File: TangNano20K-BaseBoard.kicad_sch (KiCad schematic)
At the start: 0 parts

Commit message: Add electronic schematic
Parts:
- added D1, D2, D3, D4: LED, symbol Device:LED
- added J1, J2: Conn_01x20_Socket, symbol Connector:Conn_01x20_Socket
- added J3, J4: Conn_01x06_Socket, symbol Connector:Conn_01x06_Socket
- added Q1, Q2, Q3, Q4: PN2222A, Package_TO_SOT_THT:TO-92_Inline, symbol Transistor_BJT:PN2222A
- added R1, R2, R3, R4, R5, R6, R7, R8: 220R, symbol Device:R
- added R10, R11, R12, R13, R14, R15, R16, R9: 330R, symbol Device:R
- added R19, R20, R21, R22, R23, R24, R25, R26, R27, R28: 10k, symbol Device:R
- added SW1, SW2, SW3, SW4, SW9: SW_SPDT_321, symbol Switch:SW_SPDT_321
- added SW5, SW6, SW7, SW8: SW_Push, symbol Switch:SW_Push
- added U1: CC56-12EWA, Display_7Segment:CA56-12EWA, symbol Display_Character:CC56-12EWA
- added U2: SSD1306, symbol MySymbols:SSD1306
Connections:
- new net: D1.2 (A), R13.2
- new net: R27.1, R28.2, SW9.1 (C), U2.2 (VCC)
- new net: Q2.2 (B), R10.1
- new net: Q1.2 (B), R9.1
- new net: Q4.2 (B), R12.1
- new net: D4.2 (A), R16.2
- new net: Q3.2 (B), R11.1
- new net: D2.2 (A), R14.2
- new net: D3.2 (A), R15.2
- new net +3V3: J1.19 (Pin_19), J2.16 (Pin_16), J3.5 (Pin_5), J4.5 (Pin_5), SW1.2 (B), SW2.2 (B), SW3.2 (B), SW4.2 (B), SW5.1, SW6.1, SW7.1, SW8.1, SW9.2 (B)
- new net +5V: J2.1 (Pin_1)
- new net 15: J1.6 (Pin_6), R13.1
- new net 16: J1.7 (Pin_7), R14.1
- new net 17: J1.15 (Pin_15), R15.1
- new net 18: J1.18 (Pin_18), R16.1
- new net 19: J1.17 (Pin_17), R27.2, U2.3 (SCL)
- new net 20: J1.16 (Pin_16), R28.1, U2.4 (SDA)
- new net 25: J1.10 (Pin_10), R3.1
- new net 26: J1.11 (Pin_11), R4.1
- new net 27: J1.8 (Pin_8), R1.1
- new net 28: J1.9 (Pin_9), R2.1
- new net 29: J1.12 (Pin_12), R5.1
- new net 30: J1.13 (Pin_13), R6.1
- new net 31: J1.14 (Pin_14), R7.1
- new net 41: J2.6 (Pin_6), J3.2 (Pin_2)
- new net 42: J2.5 (Pin_5), R8.1
- new net 48: J2.10 (Pin_10), R12.2
- new net 49: J2.12 (Pin_12), J3.4 (Pin_4)
- new net 51: J2.9 (Pin_9), R11.2
- new net 52: J2.20 (Pin_20), J4.4 (Pin_4)
- new net 53: J2.19 (Pin_19), J4.3 (Pin_3)
- new net 54: J2.8 (Pin_8), R10.2
- new net 55: J2.11 (Pin_11), J3.3 (Pin_3)
- new net 56: J2.7 (Pin_7), R9.2
- new net 71: J2.18 (Pin_18), R19.2, SW1.1 (C)
- new net 72: J2.17 (Pin_17), R20.2, SW2.1 (C)
- new net 73: J1.1 (Pin_1), R21.2, SW3.1 (C)
- new net 74: J1.2 (Pin_2), R22.2, SW4.1 (C)
- new net 75: J1.3 (Pin_3), R23.2, SW5.2
- new net 76: J2.3 (Pin_3), R24.2, SW6.2
- new net 77: J1.5 (Pin_5), R25.2, SW7.2
- new net 79: J2.14 (Pin_14), J4.2 (Pin_2)
- new net 80: J2.4 (Pin_4), J3.1 (Pin_1)
- new net 85: J1.4 (Pin_4), R26.2, SW8.2
- new net 86: J2.13 (Pin_13), J4.1 (Pin_1)
- new net CC1: Q1.3 (C), U1.12 (CC1)
- new net CC2: Q2.3 (C), U1.9 (CC2)
- new net CC3: Q3.3 (C), U1.8 (CC3)
- new net CC4: Q4.3 (C), U1.6 (CC4)
- new net DPX: R8.2, U1.3 (DPX)
- new net GND: D1.1 (K), D2.1 (K), D3.1 (K), D4.1 (K), J1.20 (Pin_20), J2.15 (Pin_15), J2.2 (Pin_2), J3.6 (Pin_6), J4.6 (Pin_6), Q1.1 (E), Q2.1 (E), Q3.1 (E), Q4.1 (E), R19.1, R20.1, R21.1, R22.1, R23.1, R24.1, R25.1, R26.1, U2.1 (GND)
- new net a: R1.2, U1.11 (a)
- new net b: R2.2, U1.7 (b)
- new net c: R3.2, U1.4 (c)
- new net d: R4.2, U1.2 (d)
- new net e: R5.2, U1.1 (e)
- new net f: R6.2, U1.10 (f)
- new net g: R7.2, U1.5 (g)
- no-connect marks 0 -> 5
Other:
- note added: "4-Digit 7-Segment Display"
- note added: "GPIO Expansion Headers"
- note added: "OLED Display (I2C)"
- note added: "Push Buttons"
- note added: "Slide Switches"
- note added: "Tang Nano 20K Connectors"
- note added: "User LEDs"

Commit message: Add footprint for electronic element
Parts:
- J1, J2: footprint (none) -> Connector_PinSocket_2.54mm:PinSocket_1x20_P2.54mm_Vertical
- J3, J4: footprint (none) -> Connector_PinSocket_2.54mm:PinSocket_1x06_P2.54mm_Vertical
- LED_1: renamed from D1; footprint (none) -> LED_SMD:LED_0805_2012Metric_Pad1.15x1.40mm_HandSolder
- LED_2: renamed from D2; footprint (none) -> LED_SMD:LED_0805_2012Metric_Pad1.15x1.40mm_HandSolder
- LED_3: renamed from D3; footprint (none) -> LED_SMD:LED_0805_2012Metric_Pad1.15x1.40mm_HandSolder
- LED_4: renamed from D4; footprint (none) -> LED_SMD:LED_0805_2012Metric_Pad1.15x1.40mm_HandSolder
- Push_Button_1: renamed from SW5; footprint (none) -> Button_Switch_SMD:SW_Push_1TS009xxxx-xxxx-xxxx_6x6x5mm
- Push_Button_2: renamed from SW6; footprint (none) -> Button_Switch_SMD:SW_Push_1TS009xxxx-xxxx-xxxx_6x6x5mm
- Push_Button_3: renamed from SW7; footprint (none) -> Button_Switch_SMD:SW_Push_1TS009xxxx-xxxx-xxxx_6x6x5mm
- Push_Button_4: renamed from SW8; footprint (none) -> Button_Switch_SMD:SW_Push_1TS009xxxx-xxxx-xxxx_6x6x5mm
- Q1, Q2, Q3, Q4: footprint Package_TO_SOT_THT:TO-92_Inline -> Package_TO_SOT_SMD:SOT-23
- R1, R10, R11, R12, R13, R14, R15, R16, R19, R2, R20, R21, R22, R23, R24, R25, R26, R27, R28, R3, R4, R5, R6, R7, R8, R9: footprint (none) -> Resistor_SMD:R_0805_2012Metric_Pad1.20x1.40mm_HandSolder
- Slide_Switch_1: renamed from SW1; footprint (none) -> MyFootPrints:SL19121
- Slide_Switch_2: renamed from SW2; footprint (none) -> MyFootPrints:SL19121
- Slide_Switch_3: renamed from SW3; footprint (none) -> MyFootPrints:SL19121
- Slide_Switch_4: renamed from SW4; footprint (none) -> MyFootPrints:SL19121
- Slide_Switch_OLED1: renamed from SW9; footprint (none) -> MyFootPrints:SL19121
- U2: footprint (none) -> MyFootPrints:128x64OLED

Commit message: Update schematic, add new symbol, footprint and 3d model
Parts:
- removed Push_Button_1, Push_Button_2, Push_Button_3, Push_Button_4: SW_Push, Button_Switch_SMD:SW_Push_1TS009xxxx-xxxx-xxxx_6x6x5mm, symbol Switch:SW_Push
- added S1, S2, S3, S4: 1301.9315, MyFootPrints:13019319, symbol MySymbols:1301.9315
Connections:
- net +3V3: now also S1.1 (NO_1), S2.1 (NO_1), S3.1 (NO_1), S4.1 (NO_1)
- net 75: now also S1.4 (COM_2)
- net 76: now also S2.4 (COM_2)
- net 77: now also S3.4 (COM_2)
- net 85: now also S4.4 (COM_2)
- no-connect marks 5 -> 13
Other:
- moved on the sheet: R23

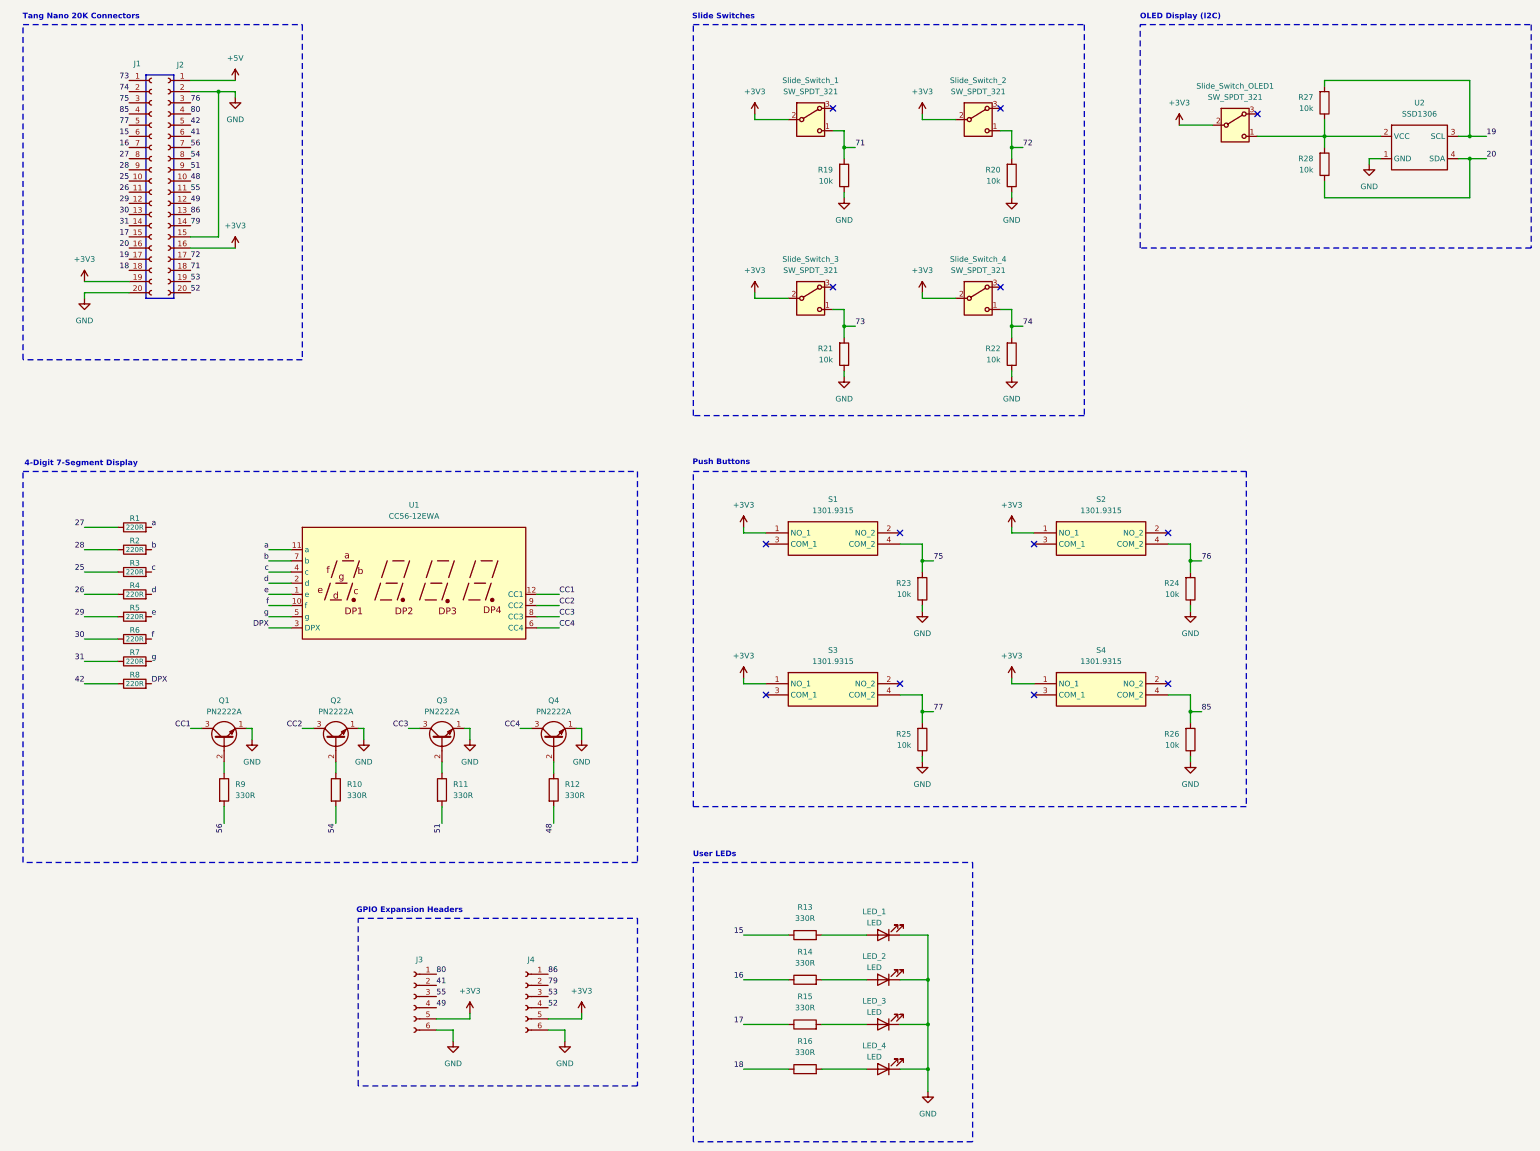
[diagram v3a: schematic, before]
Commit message: Update schematic and start design pcb layout
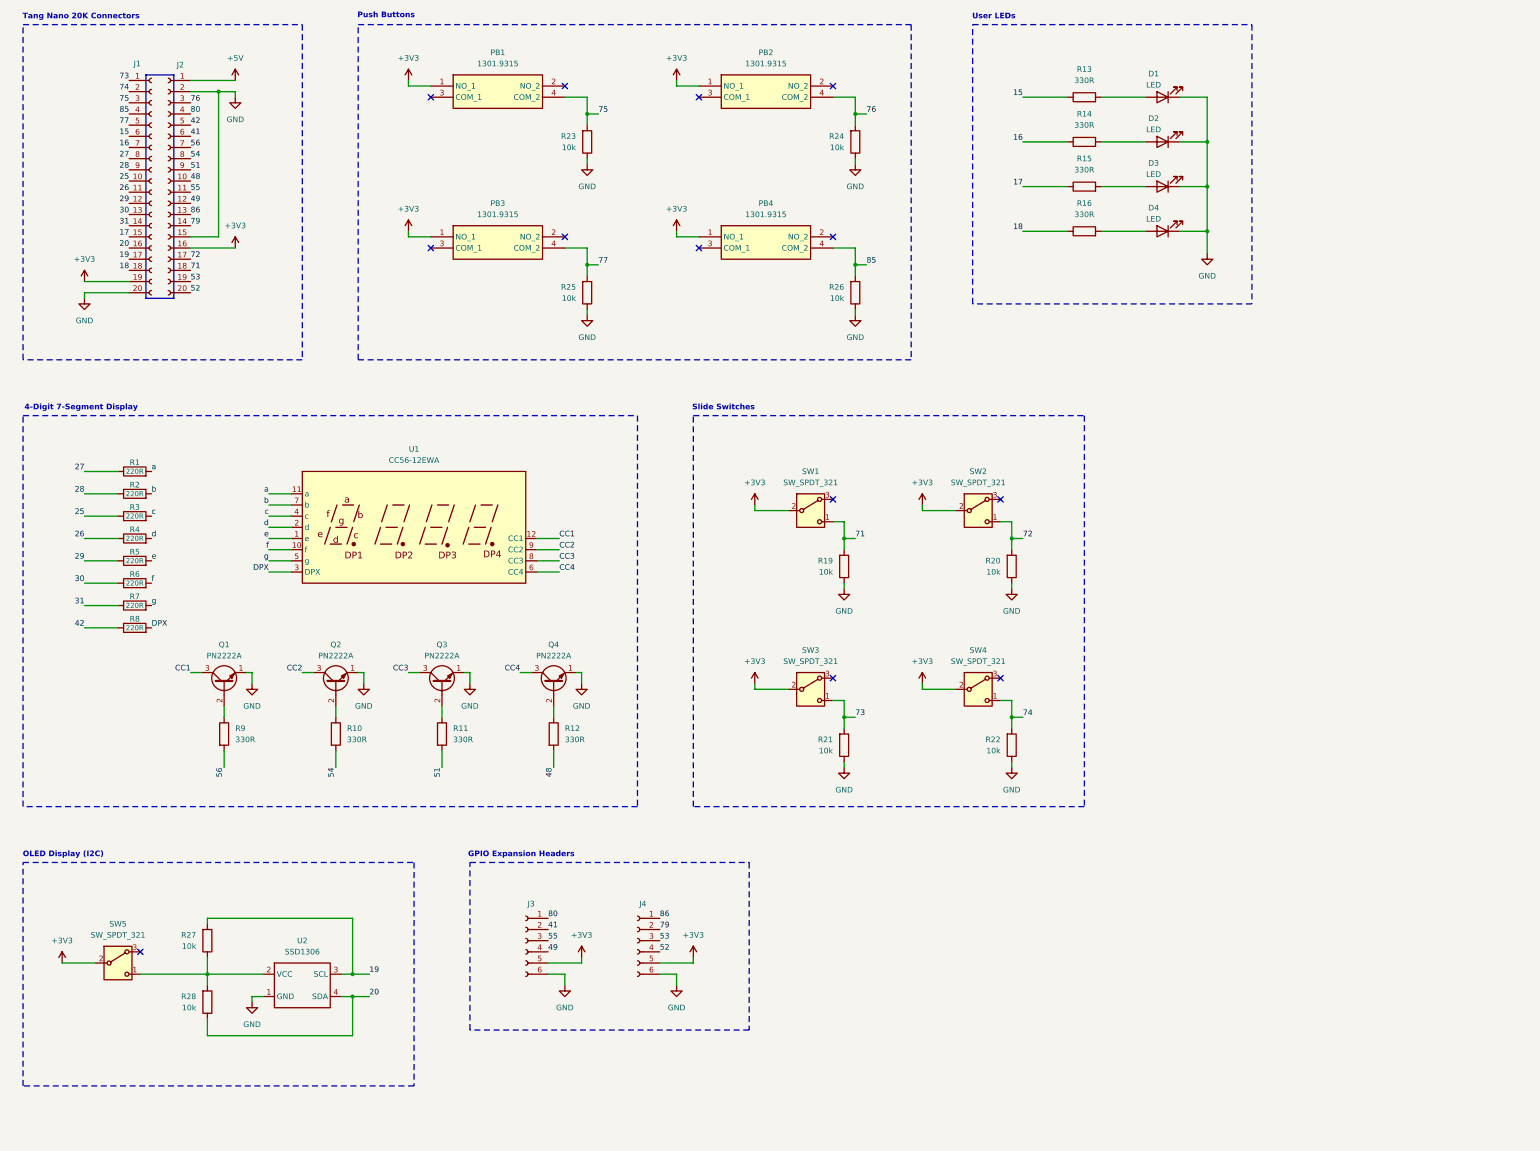
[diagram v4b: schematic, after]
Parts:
- renumbered LED_1 to D1, LED_2 to D2, LED_3 to D3, LED_4 to D4, S1 to PB1, S2 to PB2, S3 to PB3, S4 to PB4, Slide_Switch_1 to SW1, Slide_Switch_2 to SW2, Slide_Switch_3 to SW3, Slide_Switch_4 to SW4, Slide_Switch_OLED1 to SW5
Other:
- moved on the sheet: D1, D2, D3, D4, J3, J4, PB1, PB2, PB3, PB4, Q1, Q2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

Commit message: Update schematic and pcb
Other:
- moved on the sheet: R23, R28

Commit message: Big Update
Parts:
- removed J3, J4: Conn_01x06_Socket, Connector_PinSocket_2.54mm:PinSocket_1x06_P2.54mm_Vertical, symbol Connector:Conn_01x06_Socket
- added J3: Conn_02x06_Odd_Even, Connector_PinSocket_2.54mm:PinSocket_2x06_P2.54mm_Horizontal, symbol Connector_Generic:Conn_02x06_Odd_Even
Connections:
- net +3V3: now also J3.1 (Pin_1), J3.2 (Pin_2)
- net 41: now also J3.7 (Pin_7)
- net 49: now also J3.11 (Pin_11)
- net 52: now also J3.12 (Pin_12)
- net 53: now also J3.10 (Pin_10)
- net 55: now also J3.9 (Pin_9)
- net 79: now also J3.8 (Pin_8)
- net 80: now also J3.5 (Pin_5)
- net 86: now also J3.6 (Pin_6)
- net GND: now also J3.3 (Pin_3), J3.4 (Pin_4)
